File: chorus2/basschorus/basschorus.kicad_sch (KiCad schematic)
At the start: 33 parts, among them J2 IN, J4 OUT, J5 Jack-DC, SW1 SW_3PDT_x3, U3 LM337_TO220, U3 MAX1044, U4 LM317_TO-220, U5 LM317_TO-220, U6 TL074, U7 TL074

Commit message: code implementation
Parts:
- added C28, C29: 100n, Capacitor_SMD:C_0805_2012Metric, symbol Device:C
- added D1: LED, symbol Device:LED
- added R34: 3.3k, Resistor_SMD:R_0805_2012Metric, symbol Device:R
- added R_BLEND: B1M, kicad-legacy/kicad-footprints/Potentiometer_THT.pretty:Potentiometer_Alps_RK09K_Single_Vertical, symbol Device:R_Potentiometer
- added unit 2 of SW1
- added unit 5 of U1
- added unit 5 of U4
- U4: renamed from U7; footprint kicad-legacy/kicad-footprints/Package_DIP.pretty:DIP-14_W7.62mm -> (none)
- renumbered C4 to C1, C1 to C2, C15 to C3, C5 to C4, C7 to C5, C9 to C6, C11 to C7, C12 to C8, J2 to J1, J5 to J2, J4 to J3, R6 to R1, R26 to R10, R13 to R11, R14 to R12, R15 to R13, R16 to R14, R10 to R2, R7 to R3, R8 to R4, R1 to R5, R2 to R6, R9 to R7, R6 to R8, R7 to R9, U6 to U1, U5 to U2, U4 to U5, U3 to U6
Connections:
- net +7.5V: now also C28.1, C29.1, U1.4 (V+), U4.4 (V+)
- net +9V: now also R34.1, SW1.6 (C)
- net -7.5V: now also C28.2, C29.2, U1.11 (V-), U4.11 (V-)
- net GND: now also J1.R, J1.RN, J3.R, J3.RN, J3.S, J3.SN, J3.TN, R_FLANGE1.1, U4.12 (+), D1.1 (K); no longer R_FLANGE1.3
- net at R1.1: now also R_FLANGE1.3; no longer R_FLANGE1.1
- net at R1.2, R10.1, SW1.7 (A): now also U4.14; no longer U4.1
- net at R10.2, R7.1, R8.1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: now also U4.13 (-); no longer U4.2 (-)
- removed net GNDA: J3.S, J3.SN, J3.TN, U4.3 (+)
- new net: R9.2, R_BLEND.1
- new net: R_BLEND.2, SW1.1 (A)
- new net: R34.2, SW1.5 (B)
- new net: R3.2, R_BLEND.3
- new net: D1.2 (A), SW1.4 (A)
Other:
- moved on the sheet: J1, SW1A

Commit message: update filters
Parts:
- renumbered C29 to C1, C8 to C10, C28 to C2, C1 to C3, C2 to C4, C3 to C5, C4 to C6, C5 to C7, C6 to C8, C7 to C9, R9 to R10, R10 to R11, R11 to R12, R12 to R13, R13 to R14, R14 to R15, R34 to R4, R4 to R5, R5 to R6, R6 to R7, R7 to R8, R8 to R9, R_BLEND to R_BLEND1, U4 to U2, U2 to U3, U3 to U4
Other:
- note added: "https://www.reddit.com/r/diypedals/comments/12wgv4x/something_exciting_compressor_circuit_without/"
- note added: "opamps=1, inverting"
- note added: "opamps=2,inverting"
- note added: "sum half full dry signal plus half wet signal (filtered + delayed signal plus remaining signal)"
- note removed: "TODO: addative, not blended"
- note removed: "TODO: reassign opamps"
- note removed: "opamps=1"
- note removed: "opamps=2"
- note removed: "sum half full dry signal plus half wet signal (filtered + delayed signal plus remaining signal) TODO: wet/dry mix?"

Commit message: update plan based on max simulations
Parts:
- removed R_BLEND1: B1M, kicad-legacy/kicad-footprints/Potentiometer_THT.pretty:Potentiometer_Alps_RK09K_Single_Vertical, symbol Device:R_Potentiometer
- added C33: 100n, Capacitor_SMD:C_0805_2012Metric, symbol Device:C
- added U9: TL074, symbol Amplifier_Operational:TL074
- RV?: renamed from R_FLANGE1; value B1M -> R_FLANGE_B1M
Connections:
- net +7.5V: now also C33.1, U9.4 (V+)
- net -7.5V: now also C33.2, U9.11 (V-)
- net at R10.2: now also R3.2, SW1.1 (A)
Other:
- added sheet Compressor (compressor.kicad_sch)
- note added: "Datasheet recommends 3rd order AA filter with a cutoff at the nyquist limit (example from datasheet, fc=15k for a 30khz min clock). Their variant has a 5-6db passband ripple. That gives -15db at 30kHz. -- AA filter recommends 5th order at the same cutoffs. An 8K filter cutoff sounds great, a 4k sounds weaker but still has some character. Conclusion: can't be done with 512 stages, need 1024. Set m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"
- note added: "TODO: 0.2Hz is a sweet spot for the LFO. 1.2Hz is kinda cray delay sweet spot: 10-20ms These filters assuming 15kHz clock min with 1024 stages tone filter: 4.477Hz butterworth LP, 10-1kHz HP Q=0.5 AA: 3rd order butterworth LP (7080Hz?) R: 5th order butterworth LP (4477Hz) Hardcode 50/50 wet/dry flange is subtle but still worthwhile. limit to 50% resolution of 512 steps may be too low increasing w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"
- note added: "TODO: if extra opamp, buffer here"
- note added: "opamps=2..4"
- note added: "there's no good way to do a blend with an even volume unless you use a dual VCA. Even additional buffers won't cause an even blend in volume due to log taper approximations. this circuit provides several ways to control the "amount" of chorus (depth, highpass) that a true blend knob is unnecessary. instead we use a hard-coded 50% blend."
- note removed: "TODO: compressor?"
- note removed: "https://www.reddit.com/r/diypedals/comments/12wgv4x/something_exciting_compressor_circuit_without/"
- note removed: "sum half full dry signal plus half wet signal (filtered + delayed signal plus remaining signal)"
- moved on the sheet: R10, R11, R8, R9, U2D

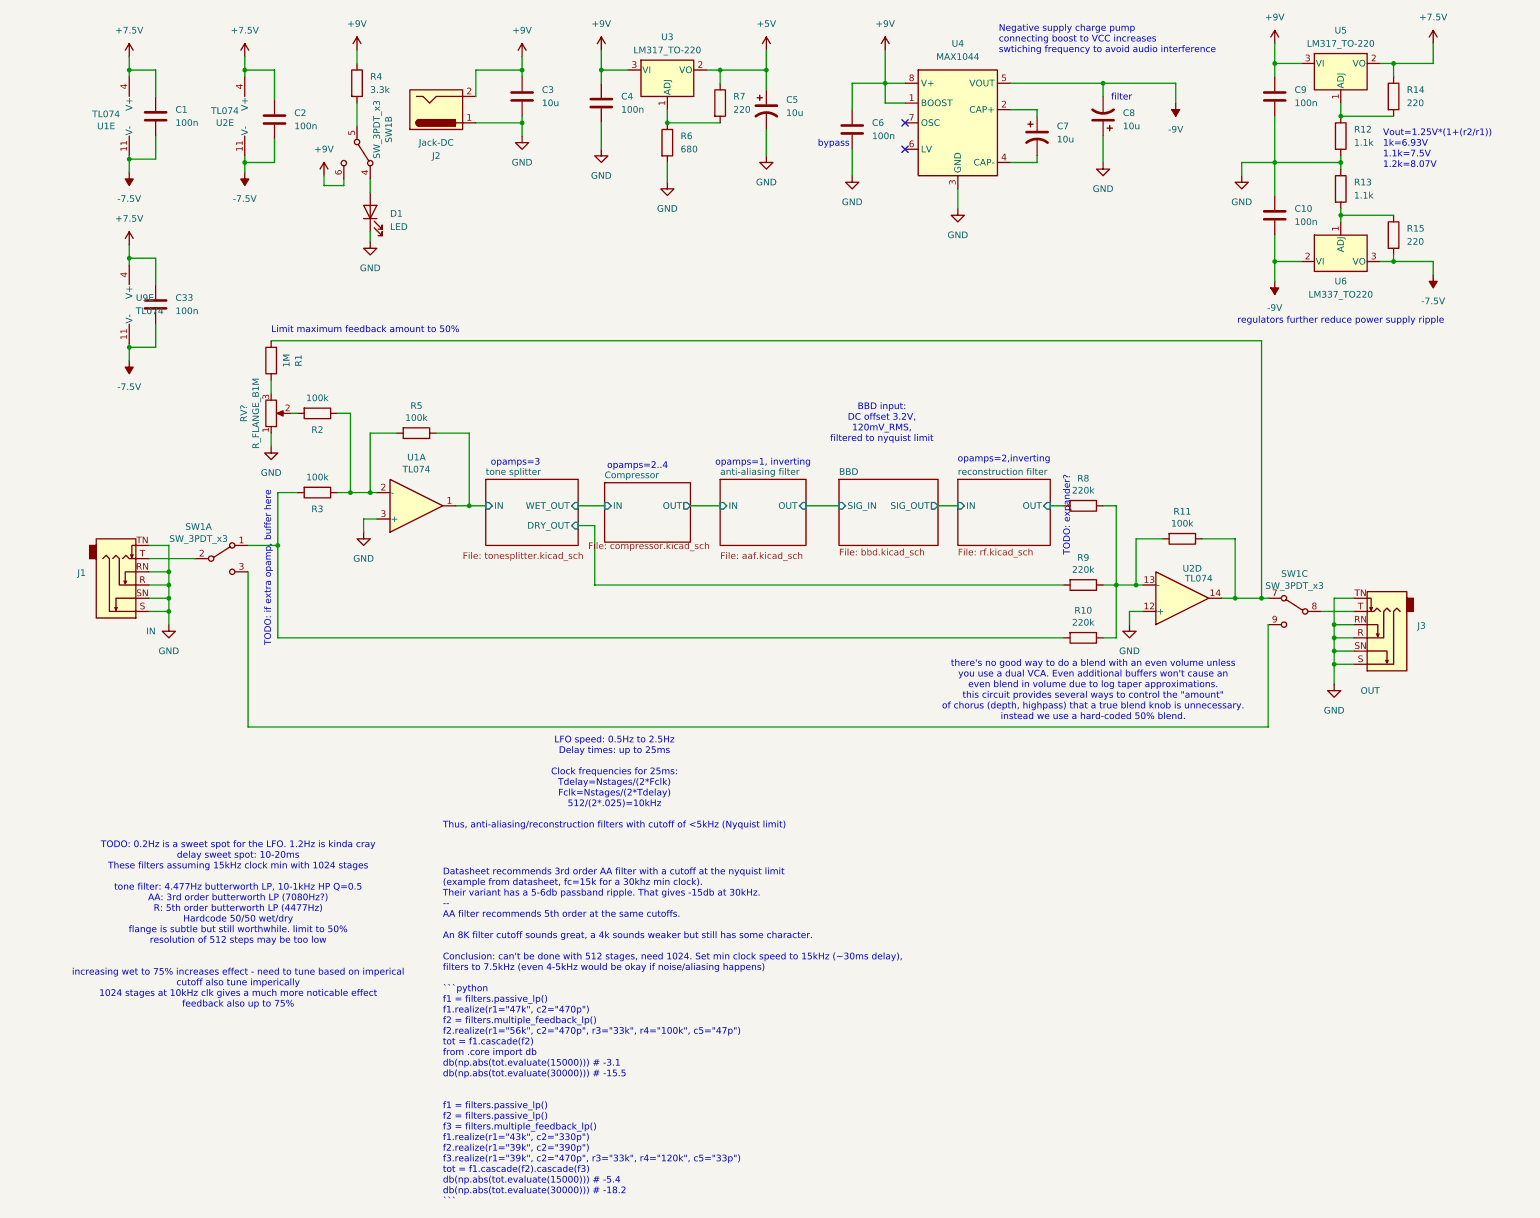
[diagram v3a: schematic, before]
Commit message: update designs based on new calculations
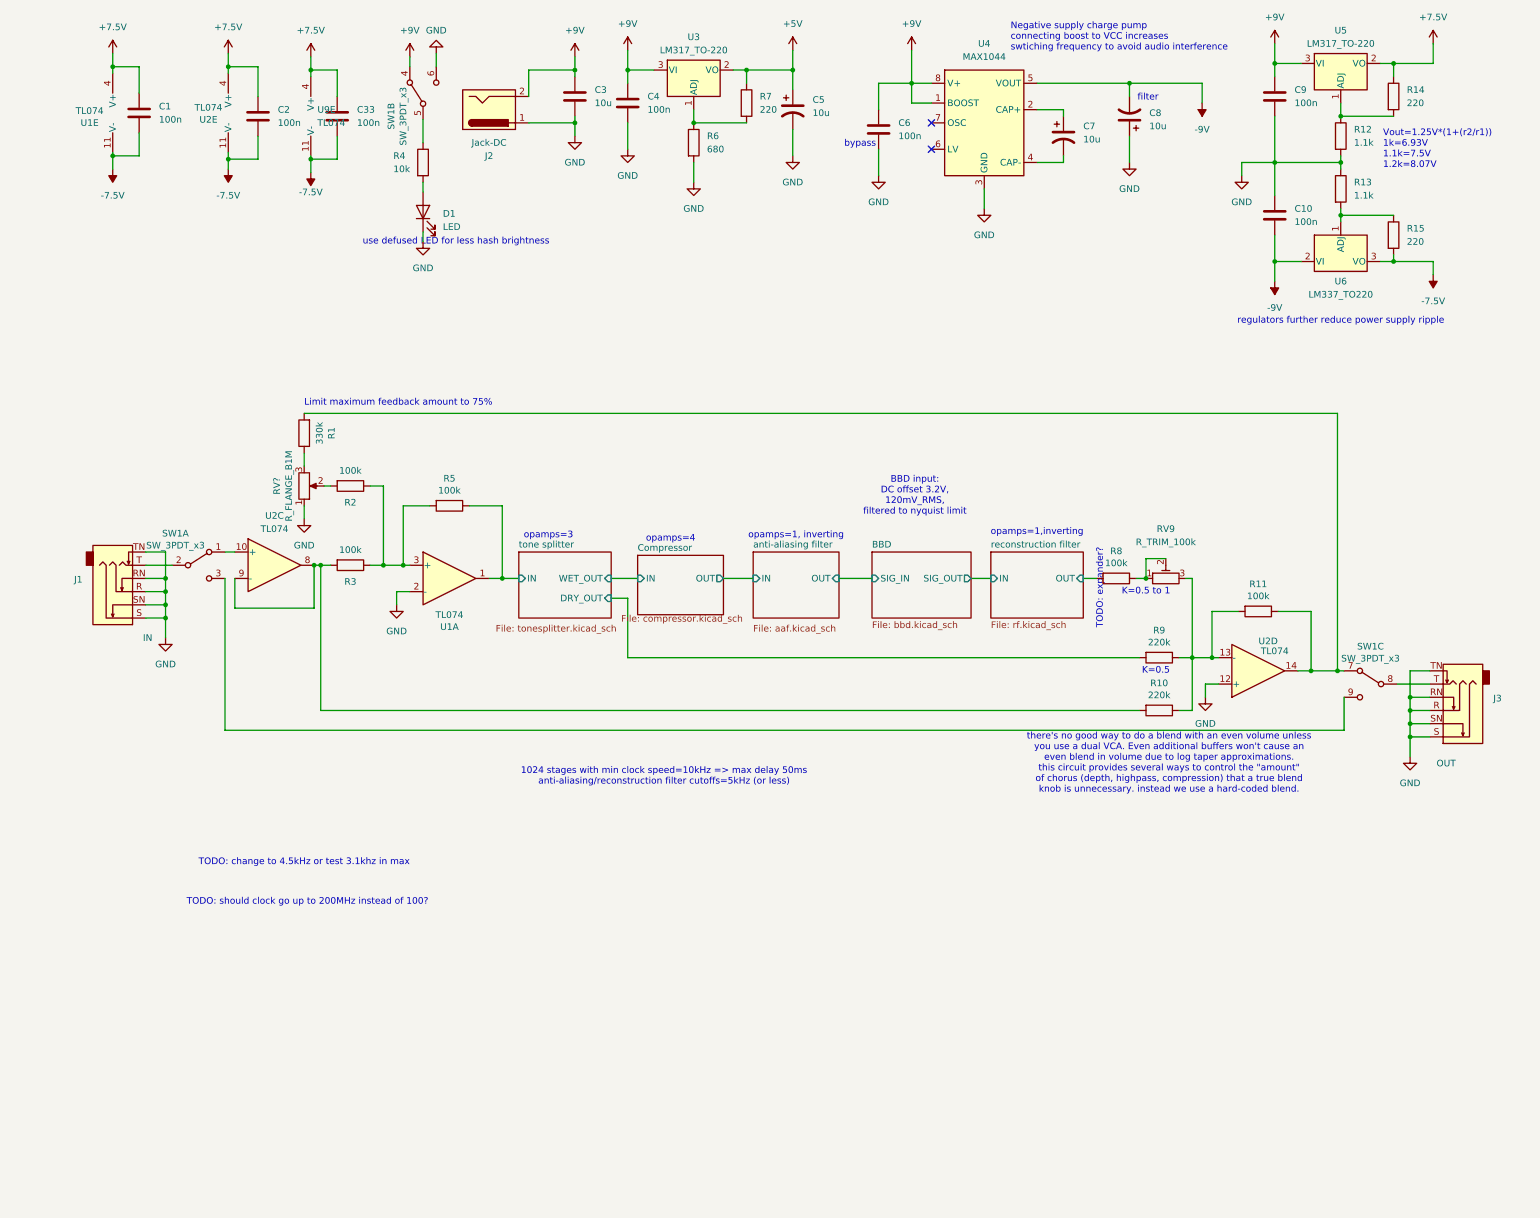
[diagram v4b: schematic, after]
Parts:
- added RV9: R_TRIM_100k, symbol Device:R_Potentiometer_Trim
- added unit 3 of U2
- R1: value 1M -> 330k
- R4: value 3.3k -> 10k
- R8: value 220k -> 100k
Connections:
- net +9V: now also SW1.4 (A); no longer R4.1, SW1.6 (C)
- net GND: now also SW1.6 (C), U1.2 (-); no longer U1.3 (+)
- net at R10.1, R11.2, R9.1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: now also RV9.3; no longer R8.1
- net at R10.2, R3.2: now also U2.8, U2.9 (-); no longer SW1.1 (A)
- net at SW1.5 (B): now also R4.1; no longer R4.2
- net at R2.1, R3.1, R5.2: now also U1.3 (+); no longer U1.2 (-)
- net at D1.2 (A): now also R4.2; no longer SW1.4 (A)
- new net: SW1.1 (A), U2.10 (+)
- new net: R8.1, RV9.1, RV9.2
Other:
- note added: "1024 stages with min clock speed=10kHz => max delay 50ms anti-aliasing/reconstruction filter cutoffs=5kHz (or less)"
- note added: "K=0.5"
- note added: "K=0.5 to 1"
- note added: "Limit maximum feedback amount to 75%"
- note added: "TODO: change to 4.5kHz or test 3.1khz in max"
- note added: "TODO: should clock go up to 200MHz instead of 100?"
- note added: "opamps=1,inverting"
- note added: "opamps=4"
- note added: "there's no good way to do a blend with an even volume unless you use a dual VCA. Even additional buffers won't cause an even blend in volume due to log taper approximations. this circuit provides several ways to control the "amount" of chorus (depth, highpass, compression) that a true blend knob is unnecessary. instead we use a hard-coded blend."
- note added: "use defused LED for less hash brightness"
- note removed: "Datasheet recommends 3rd order AA filter with a cutoff at the nyquist limit (example from datasheet, fc=15k for a 30khz min clock). Their variant has a 5-6db passband ripple. That gives -15db at 30kHz. -- AA filter recommends 5th order at the same cutoffs. An 8K filter cutoff sounds great, a 4k sounds weaker but still has some character. Conclusion: can't be done with 512 stages, need 1024. Set m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"
- note removed: "LFO speed: 0.5Hz to 2.5Hz Delay times: up to 25ms Clock frequencies for 25ms: Tdelay=Nstages/(2*Fclk) Fclk=Nstages/(2*Tdelay) 512/(2*.025)=10kHz Thus, anti-aliasing/reconstruction filters with cutoff of <5kHz (Nyquist limit)"
- note removed: "Limit maximum feedback amount to 50%"
- note removed: "TODO: 0.2Hz is a sweet spot for the LFO. 1.2Hz is kinda cray delay sweet spot: 10-20ms These filters assuming 15kHz clock min with 1024 stages tone filter: 4.477Hz butterworth LP, 10-1kHz HP Q=0.5 AA: 3rd order butterworth LP (7080Hz?) R: 5th order butterworth LP (4477Hz) Hardcode 50/50 wet/dry flange is subtle but still worthwhile. limit to 50% resolution of 512 steps may be too low increasing w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"
- note removed: "TODO: if extra opamp, buffer here"
- note removed: "opamps=2,inverting"
- note removed: "opamps=2..4"
- note removed: "there's no good way to do a blend with an even volume unless you use a dual VCA. Even additional buffers won't cause an even blend in volume due to log taper approximations. this circuit provides several ways to control the "amount" of chorus (depth, highpass) that a true blend knob is unnecessary. instead we use a hard-coded 50% blend."
- moved on the sheet: C1, C2, C3, C33, C4, C5, C6, C7, C8, D1, J1, J2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

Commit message: assign parts for testing
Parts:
- added TP11, TP12, TP15, TP16, TP17, TP18, TP19, TP2, TP20, TP21, TP22, TP3, TP5, TP6: TestPoint, TestPoint:TestPoint_THTPad_2.5x2.5mm_Drill1.2mm, symbol Connector:TestPoint
- C1, C2: footprint Capacitor_SMD:C_0805_2012Metric -> Capacitor_THT:C_Rect_L7.0mm_W2.5mm_P5.00mm
- C10: renamed from C9; footprint Capacitor_SMD:C_0805_2012Metric -> Capacitor_THT:C_Rect_L7.0mm_W2.5mm_P5.00mm
- C11: renamed from C10; footprint Capacitor_SMD:C_0805_2012Metric -> Capacitor_THT:C_Rect_L7.0mm_W2.5mm_P5.00mm
- C3: renamed from C33; footprint Capacitor_SMD:C_0805_2012Metric -> Capacitor_THT:C_Rect_L7.0mm_W2.5mm_P5.00mm
- C4: renamed from C3; footprint Capacitor_SMD:CP_Elec_5x3 -> Capacitor_THT:CP_Radial_D8.0mm_P5.00mm
- C5: renamed from C4; footprint Capacitor_SMD:C_0805_2012Metric -> Capacitor_THT:C_Rect_L7.0mm_W2.5mm_P5.00mm
- C6: renamed from C5; footprint Capacitor_SMD:CP_Elec_5x3 -> Capacitor_THT:CP_Radial_D8.0mm_P5.00mm
- C7: renamed from C6; footprint Capacitor_SMD:C_0805_2012Metric -> Capacitor_THT:C_Rect_L7.0mm_W2.5mm_P5.00mm
- C8: renamed from C7; footprint Capacitor_SMD:CP_Elec_5x3 -> Capacitor_THT:CP_Radial_D8.0mm_P5.00mm
- C9: renamed from C8; footprint Capacitor_SMD:CP_Elec_5x3 -> Capacitor_THT:CP_Radial_D8.0mm_P5.00mm
- D1: footprint (none) -> LED_THT:LED_Rectangular_W5.0mm_H2.0mm
- J1, J3: footprint kicad-legacy/kicad-footprints/Connector_Audio.pretty:Jack_6.35mm_Neutrik_NMJ6HCD2_Horizontal -> _effects_shared_footprints:Jack_6.35mm_Neutrik_NMJ6HCD3_Horizontal
- R1, R10, R11, R2, R3, R5, R8, R9: footprint kicad-legacy/kicad-footprints/Resistor_THT.pretty:R_Axial_DIN0204_L3.6mm_D1.6mm_P2.54mm_Vertical -> Resistor_THT:R_Axial_DIN0204_L3.6mm_D1.6mm_P5.08mm_Horizontal
- R12, R13, R14, R15, R4, R6, R7: footprint Resistor_SMD:R_0805_2012Metric -> Resistor_THT:R_Axial_DIN0204_L3.6mm_D1.6mm_P5.08mm_Horizontal
- RV1: renamed from RV?; footprint kicad-legacy/kicad-footprints/Potentiometer_THT.pretty:Potentiometer_Alps_RK09K_Single_Vertical -> Potentiometer_THT:Potentiometer_Alpha_RD901F-40-00D_Single_Vertical_CircularHoles
- RV2: renamed from RV9; footprint (none) -> Potentiometer_THT:Potentiometer_Vishay_T73YP_Vertical
- SW1: footprint (none) -> _effects_shared_footprints:Stompbox Switch
- U1, U2: footprint kicad-legacy/kicad-footprints/Package_DIP.pretty:DIP-14_W7.62mm -> Package_SO:SO-14_3.9x8.65mm_P1.27mm
- U2: footprint (none) -> Package_SO:SO-14_3.9x8.65mm_P1.27mm
- U3: renamed from U9; footprint (none) -> Package_SO:SO-14_3.9x8.65mm_P1.27mm
- U5: renamed from U4; footprint Package_SO:SOIC-8_3.9x4.9mm_P1.27mm -> Package_DIP:DIP-8_W7.62mm
- renumbered U3 to U4, U5 to U6, U6 to U7
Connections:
- net +5V: now also TP19.1
- net +7.5V: now also TP21.1
- net +9V: now also TP20.1
- net -7.5V: now also TP22.1
- net BBD/SIG_IN: now also TP12.1
- net BBD/SIG_OUT: now also TP15.1
- net Compressor/IN: now also TP5.1
- net Compressor/OUT: now also TP11.1
- net reconstruction filter/OUT: now also TP16.1
- net tone splitter/DRY_OUT: now also TP6.1
- net tone splitter/IN: now also TP3.1
- net at R2.2, RV1.2: now also TP17.1
- net at R1.2, R11.1, SW1.7 (A)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: now also TP18.1
- net at R10.2, R3.2, U2.8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: now also TP2.1

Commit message: started layout
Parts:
- TP11: value TestPoint -> COMP
- TP12: value TestPoint -> AA
- TP15: value TestPoint -> BBD2
- TP16: value TestPoint -> RF
- TP17: value TestPoint -> FLANGE
- TP18: value TestPoint -> OUT
- TP19: value TestPoint -> 5V
- TP2: value TestPoint -> IN
- TP20: value TestPoint -> 9V
- TP21: value TestPoint -> +7.5V
- TP22: value TestPoint -> -7.5V
- TP3: value TestPoint -> SUM
- TP5: value TestPoint -> TONEW
- TP6: value TestPoint -> TONED
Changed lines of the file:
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@@
 		(fields_autoplaced yes)
 		(property "Reference" "TP15"
-			(at 188.595 117.3479 0)
+			(at 187.96 117.3479 0)
 			(effects
 				(font
@@
 			)
 		)
-		(property "Value" "TestPoint"
-			(at 188.595 119.8879 0)
+		(property "Value" "BBD2"
+			(at 187.96 119.8879 0)
 			(effects
 				(font
@@
 		(fields_autoplaced yes)
 		(property "Reference" "TP3"
-			(at 95.885 123.9519 0)
+			(at 96.52 123.9519 0)
 			(effects
 				(font
@@
 			)
 		)
-		(property "Value" "TestPoint"
-			(at 95.885 126.4919 0)
+		(property "Value" "SUM"
+			(at 96.52 126.4919 0)
 			(effects
 				(font
@@
 			)
 		)
-		(property "Value" "TestPoint"
+		(property "Value" "AA"
 			(at 163.83 119.8879 0)
 			(effects
@@
 			)
 		)
-		(property "Value" "TestPoint"
+		(property "Value" "5V"
 			(at 154.94 25.3999 90)
 			(effects
@@
 		(fields_autoplaced yes)
 		(property "Reference" "TP11"
-			(at 141.605 117.3479 0)
+			(at 140.97 117.3479 0)
 			(effects
 				(font
@@
 			)
 		)
-		(property "Value" "TestPoint"
-			(at 141.605 119.8879 0)
+		(property "Value" "COMP"
+			(at 140.97 119.8879 0)
 			(effects
 				(font
@@
 		(fields_autoplaced yes)
 		(property "Reference" "TP2"
-			(at 64.135 139.6999 90)
+			(at 64.77 139.6999 90)
 			(effects
 				(font
@@
 			)
 		)
-		(property "Value" "TestPoint"
-			(at 64.135 142.2399 90)
+		(property "Value" "IN"
+			(at 64.77 142.2399 90)
 			(effects
 				(font
@@
 			)
 		)
-		(property "Value" "TestPoint"
+		(property "Value" "9V"
 			(at 113.03 25.3999 90)
 			(effects
@@
 			)
 		)
-		(property "Value" "TestPoint"
+		(property "Value" "RF"
 			(at 209.55 119.8879 0)
 			(effects
@@
 			)
 		)
-		(property "Value" "TestPoint"
+		(property "Value" "TONEW"
 			(at 119.38 119.8879 0)
 			(effects
@@
 			)
 		)
-		(property "Value" "TestPoint"
+		(property "Value" "FLANGE"
 			(at 62.23 102.1079 0)
 			(effects
@@
 		(fields_autoplaced yes)
 		(property "Reference" "TP18"
-			(at 252.095 141.7319 0)
+			(at 251.46 141.7319 0)
 			(effects
 				(font
@@
 			)
 		)
-		(property "Value" "TestPoint"
-			(at 252.095 144.2719 0)
+		(property "Value" "OUT"
+			(at 251.46 144.2719 0)
 			(effects
 				(font
@@
 			)
 		)
-		(property "Value" "TestPoint"
+		(property "Value" "-7.5V"
 			(at 278.13 62.2299 90)
 			(effects
@@
 			)
 		)
-		(property "Value" "TestPoint"
+		(property "Value" "TONED"
 			(at 128.27 135.1279 0)
 			(effects
@@
 			)
 		)
-		(property "Value" "TestPoint"
+		(property "Value" "+7.5V"
 			(at 278.13 24.1299 90)
 			(effects
